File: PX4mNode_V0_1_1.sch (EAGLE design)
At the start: 135 parts, among them J201 DF13C-6P-1.25V, J202 DF13C-6P-1.25V, J203 DF13C-6P-1.25V, J301 DF13C-4P-1.25V, J401 DF13C-7P-1.25V, J402 DF13-4P-1.25V, J403 DF13C-4P-1.25V, J404 DF13C-4P-1.25V, J405 DF13C-4P-1.25V, J801 DF13C-3P-1.25V, M3_MOUNT1101 MOUNT-HOLE3.1MM, M3_MOUNT1102 MOUNT-HOLE3.1MM, M3_MOUNT1103 MOUNT-HOLE3.1MM, M3_MOUNT1104 MOUNT-HOLE3.1MM, U101 STM32F4X7VX, U401 MAX3051, U402 MAX3051, X101 3.2x2.5 mm / 24 MHz / 15 ppm

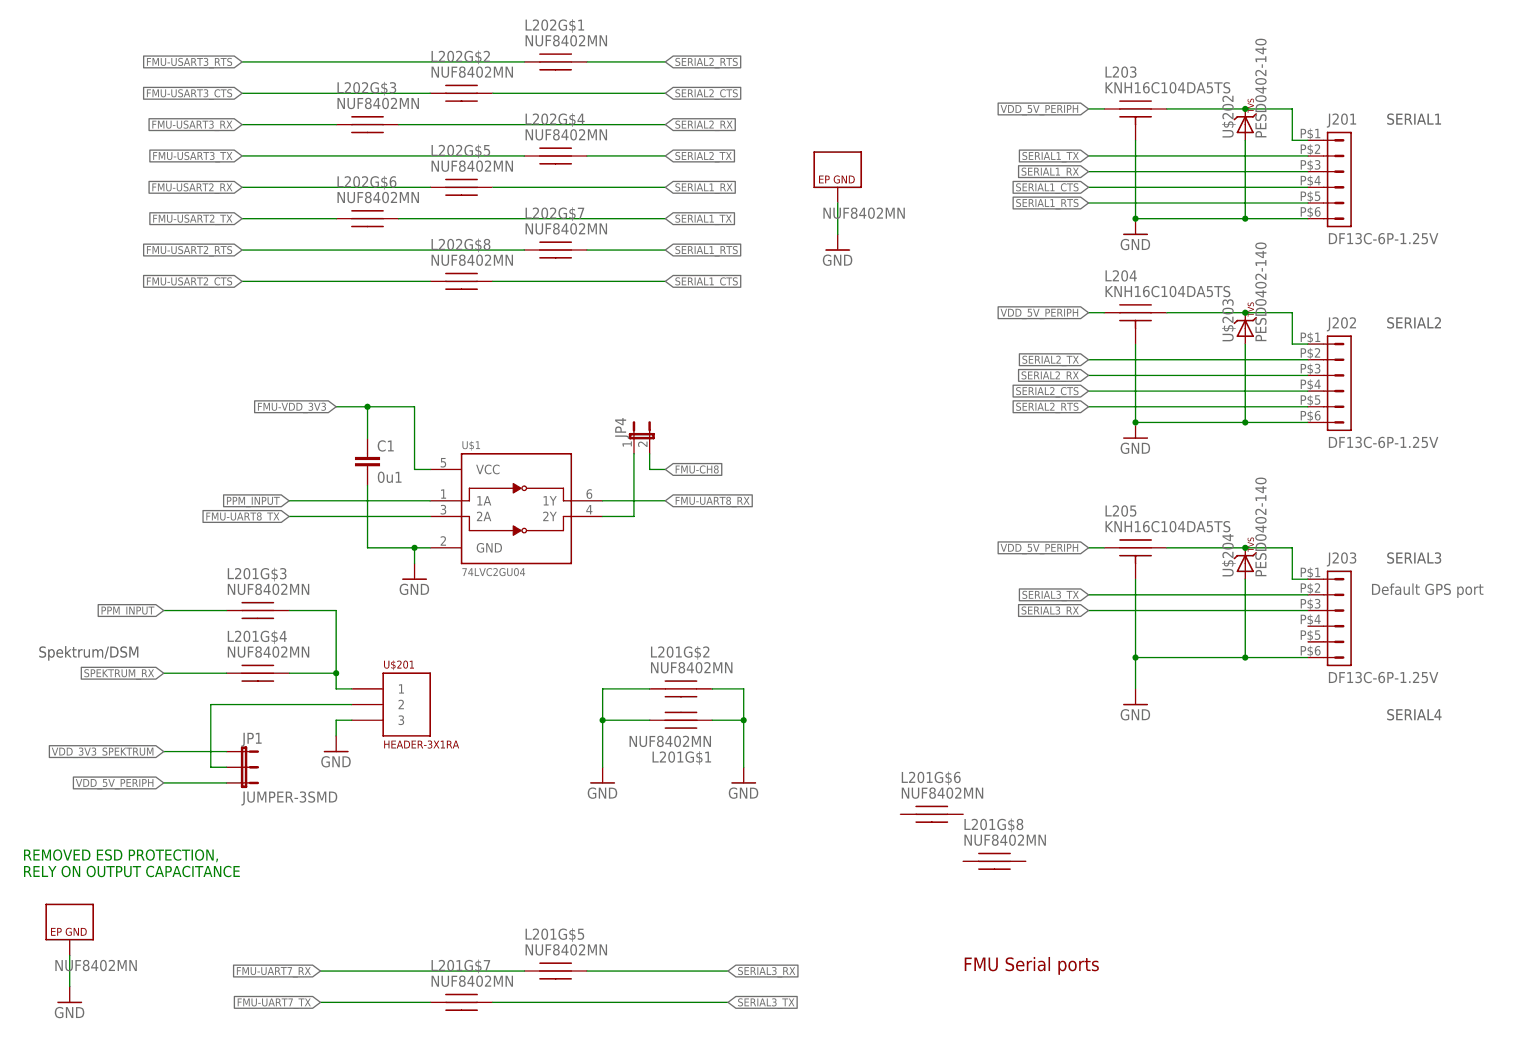
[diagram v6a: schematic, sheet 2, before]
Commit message: Part renumbering again
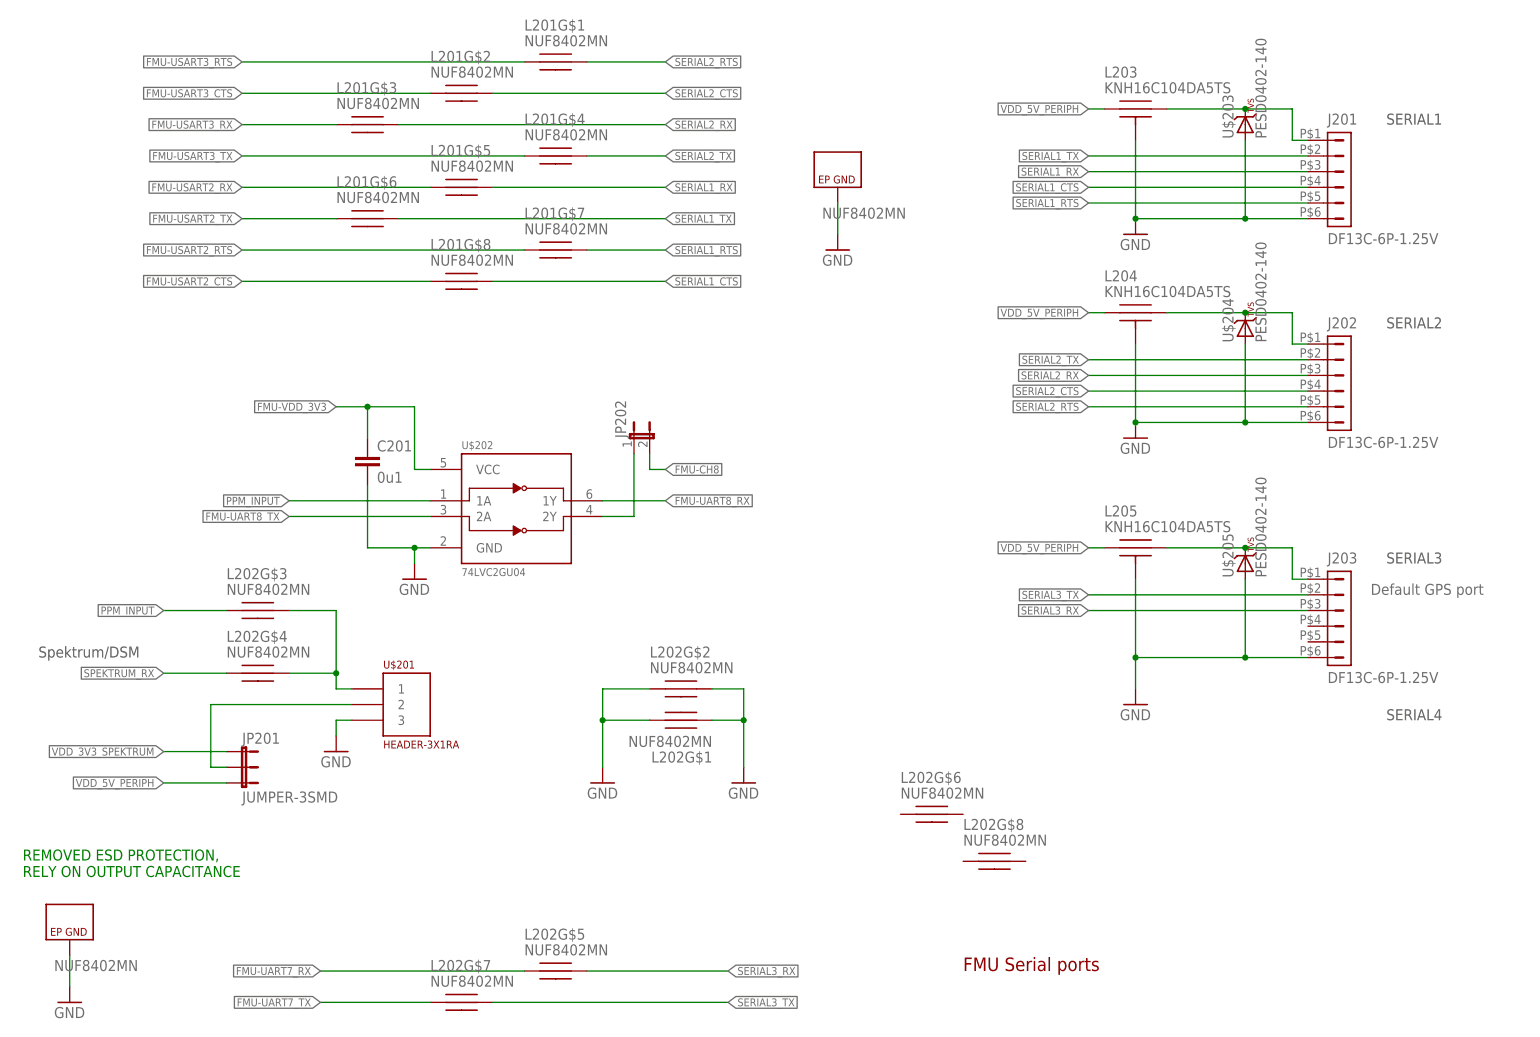
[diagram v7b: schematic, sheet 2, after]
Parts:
- removed JP2, JP3: FIDUCIAL1.5X3, pixhawk2:FIDUCIAL1.5X3
- removed U$1: 74LVC2GU04, pixhawk2:74LVC2GU04
- added JP1103, JP1104: FIDUCIAL1.5X3, pixhawk2:FIDUCIAL1.5X3
- added U$205: PESD0402-140, pixhawk2:DIODE-TVS
- U$202: value PESD0402-140 -> 74LVC2GU04; device pixhawk2:DIODE-TVS -> pixhawk2:74LVC2GU04; PARTNO PESD0402-140 -> (none)
- renumbered C1 to C201, D1 to D701, J$405 to J$401, JP1 to JP201, JP4 to JP202, U$602 to U$601
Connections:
- net 5V_S1_FILTERED: now also U$203.C; no longer U$202.C
- net 5V_S2_FILTERED: now also U$204.C; no longer U$203.C
- net 5V_S3_FILTERED: now also U$205.C; no longer U$204.C
- net FMU-UART7_RX: now also L202G$5.P$1; no longer L201G$5.P$1
- net FMU-UART7_TX: now also L202G$7.P$1; no longer L201G$7.P$1
- net FMU-UART8_RX: now also U$202.1Y; no longer U$1.1Y
- net FMU-UART8_TX: now also U$202.2A; no longer U$1.2A
- net FMU-USART2_CTS: now also L201G$8.P$1; no longer L202G$8.P$1
- net FMU-USART2_RTS: now also L201G$7.P$1; no longer L202G$7.P$1
- net FMU-USART2_RX: now also L201G$5.P$1; no longer L202G$5.P$1
- net FMU-USART2_TX: now also L201G$6.P$1; no longer L202G$6.P$1
- net FMU-USART3_CTS: now also L201G$2.P$1; no longer L202G$2.P$1
- net FMU-USART3_RTS: now also L201G$1.P$1; no longer L202G$1.P$1
- net FMU-USART3_RX: now also L201G$3.P$1; no longer L202G$3.P$1
- net FMU-USART3_TX: now also L201G$4.P$1; no longer L202G$4.P$1
- net FMU-VDD_3V3: now also R702.1, U$202.VCC; no longer R703.1, U$1.VCC
- net GND: now also L202G$1.P$1, L202G$1.P$2, L202G$2.P$1, L202G$2.P$2, R703.1, U$202.GND, U$205.A; no longer L201G$1.P$1, L201G$1.P$2, L201G$2.P$1, L201G$2.P$2, R702.1, U$1.GND, U$202.A
- net N$18: now also L202G$3.P$2, L202G$4.P$2; no longer L201G$3.P$2, L201G$4.P$2
- net N$5: now also U$202.2Y; no longer U$1.2Y
- net PPM_INPUT: now also L202G$3.P$1, U$202.1A; no longer L201G$3.P$1, U$1.1A
- net SERIAL1_CTS: now also L201G$8.P$2; no longer L202G$8.P$2
- net SERIAL1_RTS: now also L201G$7.P$2; no longer L202G$7.P$2
- net SERIAL1_RX: now also L201G$5.P$2; no longer L202G$5.P$2
- net SERIAL1_TX: now also L201G$6.P$2; no longer L202G$6.P$2
- net SERIAL2_CTS: now also L201G$2.P$2; no longer L202G$2.P$2
- net SERIAL2_RTS: now also L201G$1.P$2; no longer L202G$1.P$2
- net SERIAL2_RX: now also L201G$3.P$2; no longer L202G$3.P$2
- net SERIAL2_TX: now also L201G$4.P$2; no longer L202G$4.P$2
- net SERIAL3_RX: now also L202G$5.P$2; no longer L201G$5.P$2
- net SERIAL3_TX: now also L202G$7.P$2; no longer L201G$7.P$2
- net SPEKTRUM_RX: now also L202G$4.P$1; no longer L201G$4.P$1
- net VDD_3V3_PERIPH_EN: now also R703.2; no longer R702.2
- net VDD_3V3_SENSORS_EN: now also R702.2; no longer R703.2
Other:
- moved on the sheet: L201G$1, L201G$2, L201G$3, L201G$4, L201G$5, L201G$6, L201G$7, L201G$8, L202G$1, L202G$2, L202G$3, L202G$4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

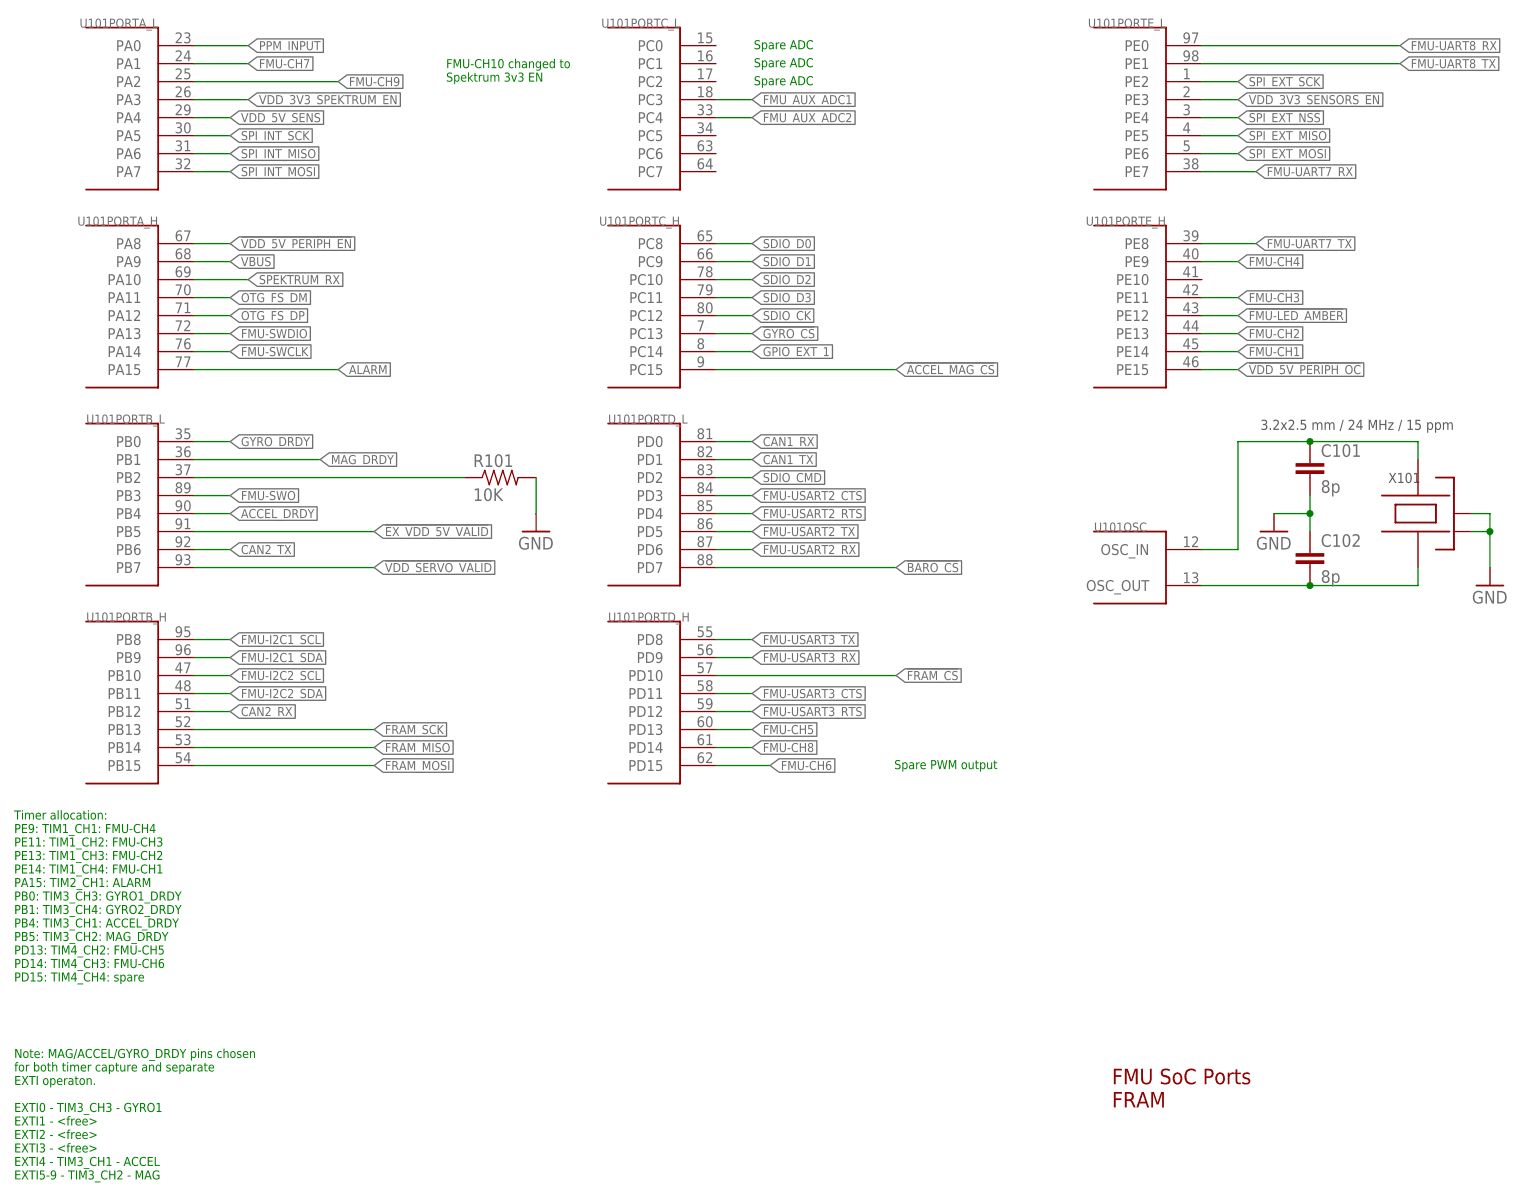
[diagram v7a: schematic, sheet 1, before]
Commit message: Moved VDD_3V3_SPEKTRUM_EN to a spare ADC to make space for FMU_CH10
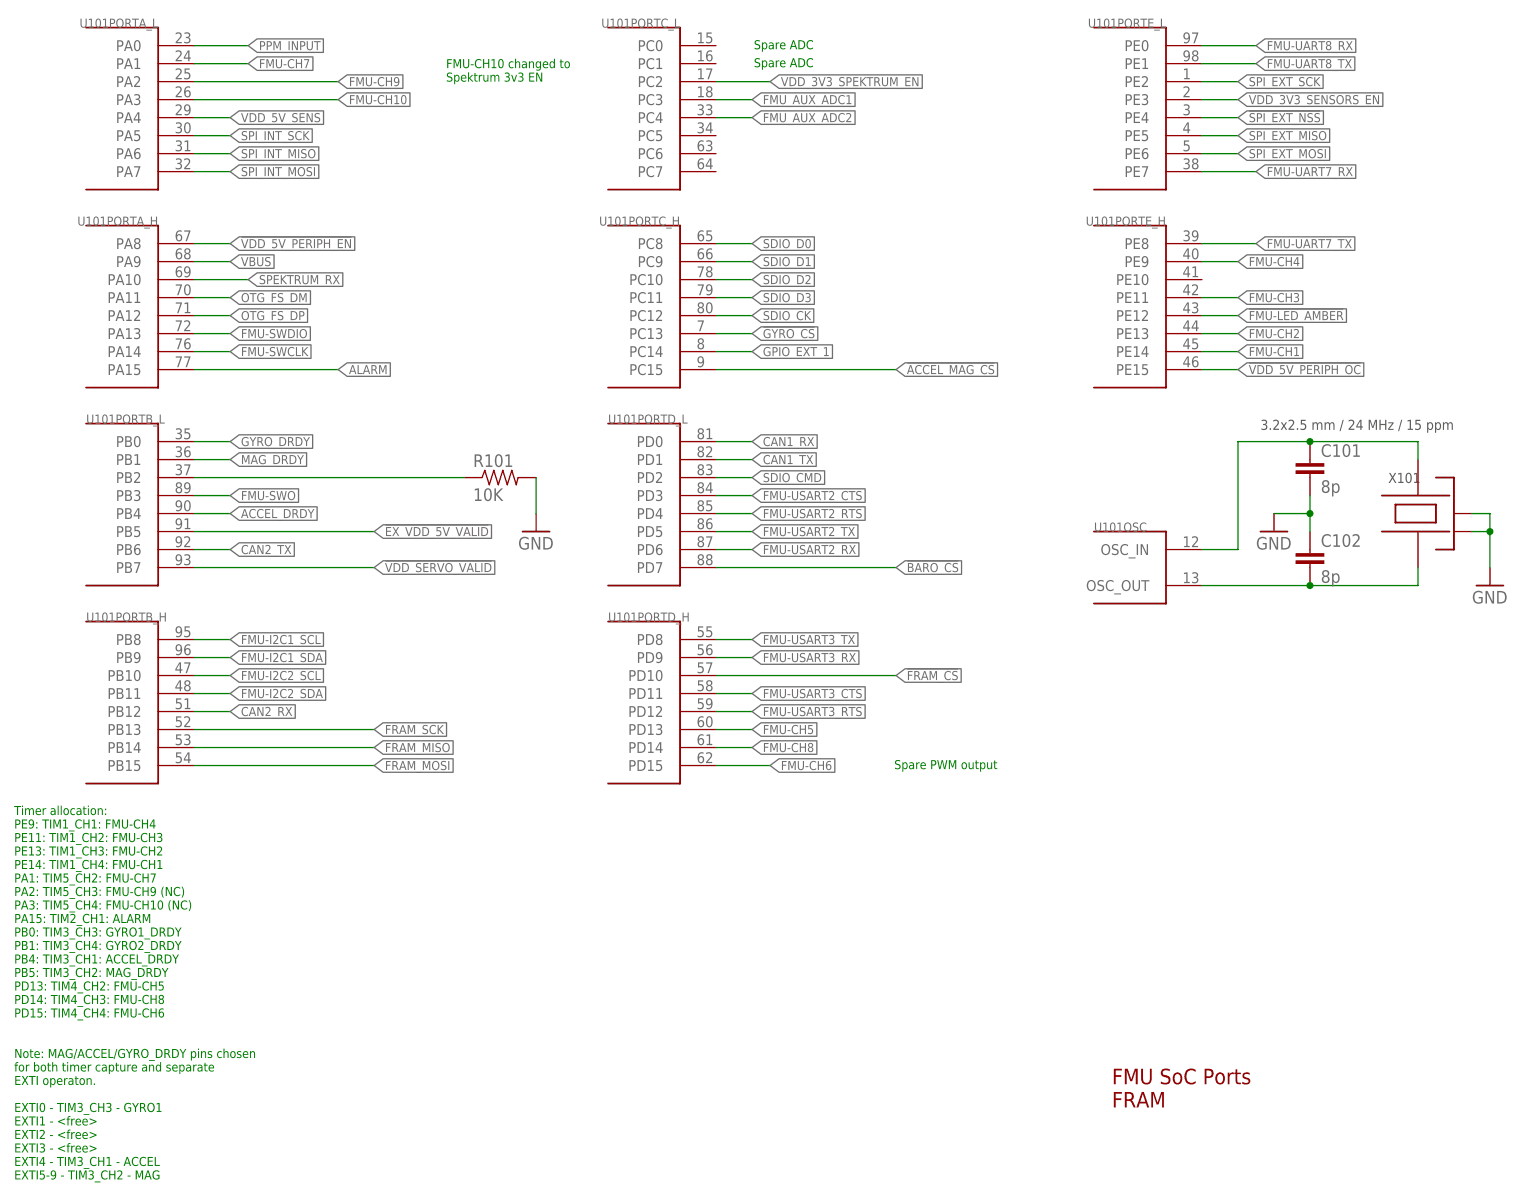
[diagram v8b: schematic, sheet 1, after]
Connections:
- new net FMU-CH10: U101PORTA_L.PA3
- net VDD_3V3_SPEKTRUM_EN: now also U101PORTC_L.PC2; no longer U101PORTA_L.PA3
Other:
- note added: "Timer allocation: PE9: TIM1_CH1: FMU-CH4 PE11: TIM1_CH2: FMU-CH3 PE13: TIM1_CH3: FMU-CH2 PE14: TIM1_CH4: FMU-CH1 PA1: TIM5_CH2: FMU-CH7 PA2: TIM5_CH3: FMU-CH9 (NC) PA3: TIM5_CH4: FMU-CH10 (NC) PA15: TIM2_CH1: ALARM PB0: TIM3_CH3: GYRO1_DRDY PB1: TIM3_CH4: GYRO2_DRDY PB4: TIM3_CH1: ACCEL_DRDY PB5: TIM3_CH2: MAG_DRDY PD13: TIM4_CH2: FMU-CH5 PD14: TIM4_CH3: FMU-CH8 PD15: TIM4_CH4: FMU-CH6"
- note removed: "Timer allocation: PE9: TIM1_CH1: FMU-CH4 PE11: TIM1_CH2: FMU-CH3 PE13: TIM1_CH3: FMU-CH2 PE14: TIM1_CH4: FMU-CH1 PA15: TIM2_CH1: ALARM PB0: TIM3_CH3: GYRO1_DRDY PB1: TIM3_CH4: GYRO2_DRDY PB4: TIM3_CH1: ACCEL_DRDY PB5: TIM3_CH2: MAG_DRDY PD13: TIM4_CH2: FMU-CH5 PD14: TIM4_CH3: FMU-CH6 PD15: TIM4_CH4: spare"
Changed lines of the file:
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@@
 EXTI5-9 - TIM3_CH2 - MAG
 </text>
-<text x="7.62" y="33.02" size="1.27" layer="91">Timer allocation:
+<text x="7.62" y="27.94" size="1.27" layer="91">Timer allocation:
 PE9: TIM1_CH1: FMU-CH4
 PE11: TIM1_CH2: FMU-CH3
 PE13: TIM1_CH3: FMU-CH2
 PE14: TIM1_CH4: FMU-CH1
+PA1: TIM5_CH2: FMU-CH7
+PA2: TIM5_CH3: FMU-CH9 (NC)
+PA3: TIM5_CH4: FMU-CH10 (NC)
 PA15: TIM2_CH1: ALARM
 PB0: TIM3_CH3: GYRO1_DRDY
@@
 PB5: TIM3_CH2: MAG_DRDY
 PD13: TIM4_CH2: FMU-CH5
-PD14: TIM4_CH3: FMU-CH6
-PD15: TIM4_CH4: spare
+PD14: TIM4_CH3: FMU-CH8
+PD15: TIM4_CH4: FMU-CH6
 </text>
 <text x="131.826" y="62.992" size="1.27" layer="91">Spare PWM output</text>
 <text x="112.014" y="164.592" size="1.27" layer="91">Spare ADC</text>
-<text x="112.014" y="159.512" size="1.27" layer="91">Spare ADC</text>
 <text x="112.014" y="162.052" size="1.27" layer="91">Spare ADC</text>
 <text x="68.58" y="160.02" size="1.27" layer="91">FMU-CH10 changed to
@@
 <segment>
 <pinref part="U101" gate="PORTE_L" pin="PE0"/>
-<wire x1="175.26" y1="165.1" x2="203.2" y2="165.1" width="0.1524" layer="91"/>
-<label x="203.2" y="165.1" size="1.27" layer="95" xref="yes"/>
+<wire x1="175.26" y1="165.1" x2="182.88" y2="165.1" width="0.1524" layer="91"/>
+<label x="182.88" y="165.1" size="1.27" layer="95" xref="yes"/>
 </segment>
 </net>
@@
 <segment>
 <pinref part="U101" gate="PORTB_L" pin="PB1"/>
-<wire x1="33.02" y1="106.68" x2="50.8" y2="106.68" width="0.1524" layer="91"/>
-<label x="50.8" y="106.68" size="1.27" layer="95" xref="yes"/>
+<wire x1="33.02" y1="106.68" x2="38.1" y2="106.68" width="0.1524" layer="91"/>
+<label x="38.1" y="106.68" size="1.27" layer="95" xref="yes"/>
 </segment>
 </net>
@@
 <segment>
 <pinref part="U101" gate="PORTE_L" pin="PE1"/>
-<wire x1="175.26" y1="162.56" x2="203.2" y2="162.56" width="0.1524" layer="91"/>
-<label x="203.2" y="162.56" size="1.27" layer="95" xref="yes"/>
+<wire x1="175.26" y1="162.56" x2="182.88" y2="162.56" width="0.1524" layer="91"/>
+<label x="182.88" y="162.56" size="1.27" layer="95" xref="yes"/>
 </segment>
 </net>
@@
 <net name="VDD_3V3_SPEKTRUM_EN" class="0">
 <segment>
-<pinref part="U101" gate="PORTA_L" pin="PA3"/>
-<wire x1="33.02" y1="157.48" x2="40.64" y2="157.48" width="0.1524" layer="91"/>
-<label x="40.64" y="157.48" size="1.27" layer="95" xref="yes"/>
+<wire x1="106.68" y1="160.02" x2="114.3" y2="160.02" width="0.1524" layer="91"/>
+<label x="114.3" y="160.02" size="1.27" layer="95" xref="yes"/>
+<pinref part="U101" gate="PORTC_L" pin="PC2"/>
 </segment>
 </net>
@@
 <wire x1="33.02" y1="165.1" x2="40.64" y2="165.1" width="0.1524" layer="91"/>
 <label x="40.64" y="165.1" size="1.27" layer="95" xref="yes"/>
+</segment>
+</net>
+<net name="FMU-CH10" class="0">
+<segment>
+<pinref part="U101" gate="PORTA_L" pin="PA3"/>
+<wire x1="33.02" y1="157.48" x2="53.34" y2="157.48" width="0.1524" layer="91"/>
+<label x="53.34" y="157.48" size="1.27" layer="95" xref="yes"/>
 </segment>
 </net>
@@
 <plain>
 <text x="165.1" y="17.78" size="2.1844" layer="94" ratio="10">Sensors</text>
-<text x="7.62" y="7.62" size="1.27" layer="97" font="vector">Bypass caps as close to device pins as possible.</text>
-<wire x1="127" y1="101.6" x2="127" y2="165.1" width="0.1524" layer="94" style="dashdot"/>
-<wire x1="127" y1="165.1" x2="5.08" y2="165.1" width="0.1524" layer="94" style="dashdot"/>
-<wire x1="5.08" y1="165.1" x2="5.08" y2="33.02" width="0.1524" layer="94" style="dashdot"/>
-<wire x1="127" y1="165.1" x2="254" y2="165.1" width="0.1524" layer="94" style="dashdot"/>
-<wire x1="254" y1="165.1" x2="254" y2="101.6" width="0.1524" layer="94" style="dashdot"/>
-<wire x1="254" y1="101.6" x2="127" y2="101.6" width="0.1524" layer="94" style="dashdot"/>
+<text x="96.52" y="33.02" size="1.27" layer="97" font="vector">Bypass caps as close to device pins as possible.</text>
 </plain>
 <instances>
